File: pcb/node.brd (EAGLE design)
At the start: 50 x 68.5 mm, 14 parts, among them J1 RJ11, J2 RJ11

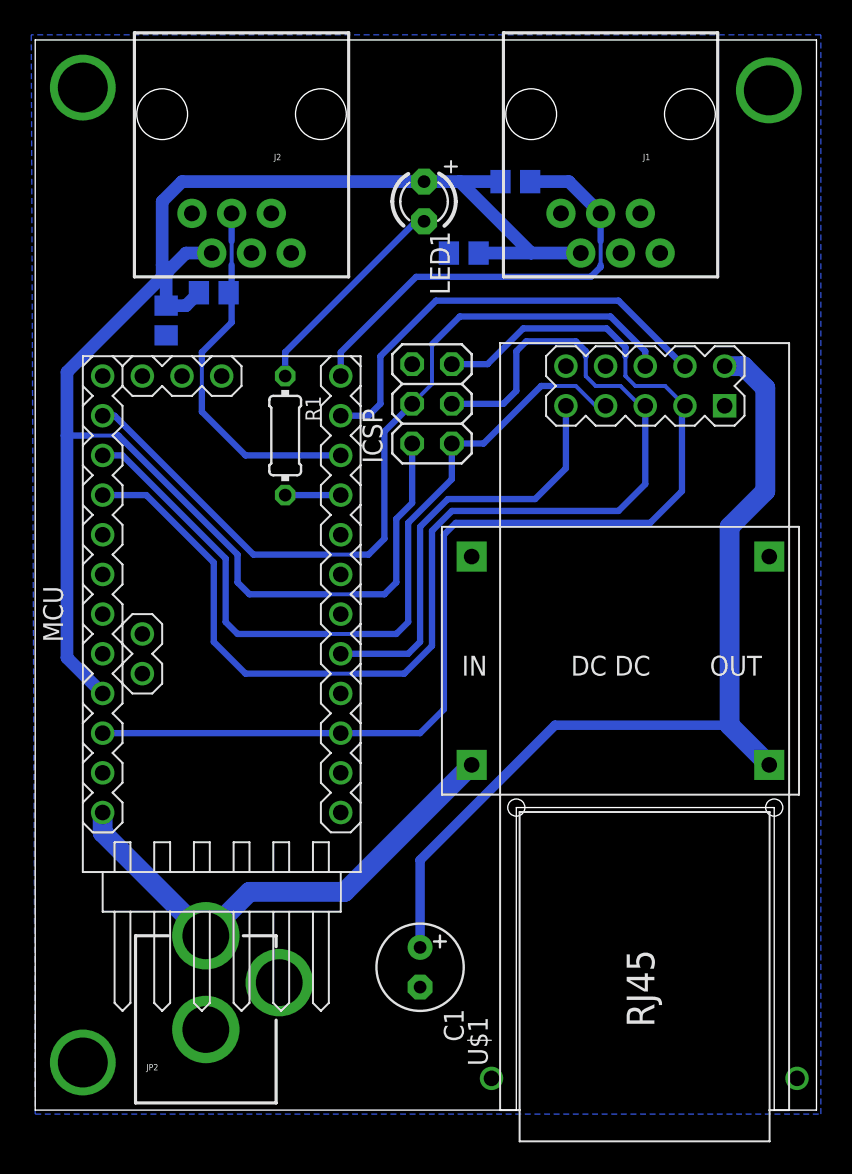
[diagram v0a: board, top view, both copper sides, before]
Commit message: New two layer board version (dirtypcbs.com).
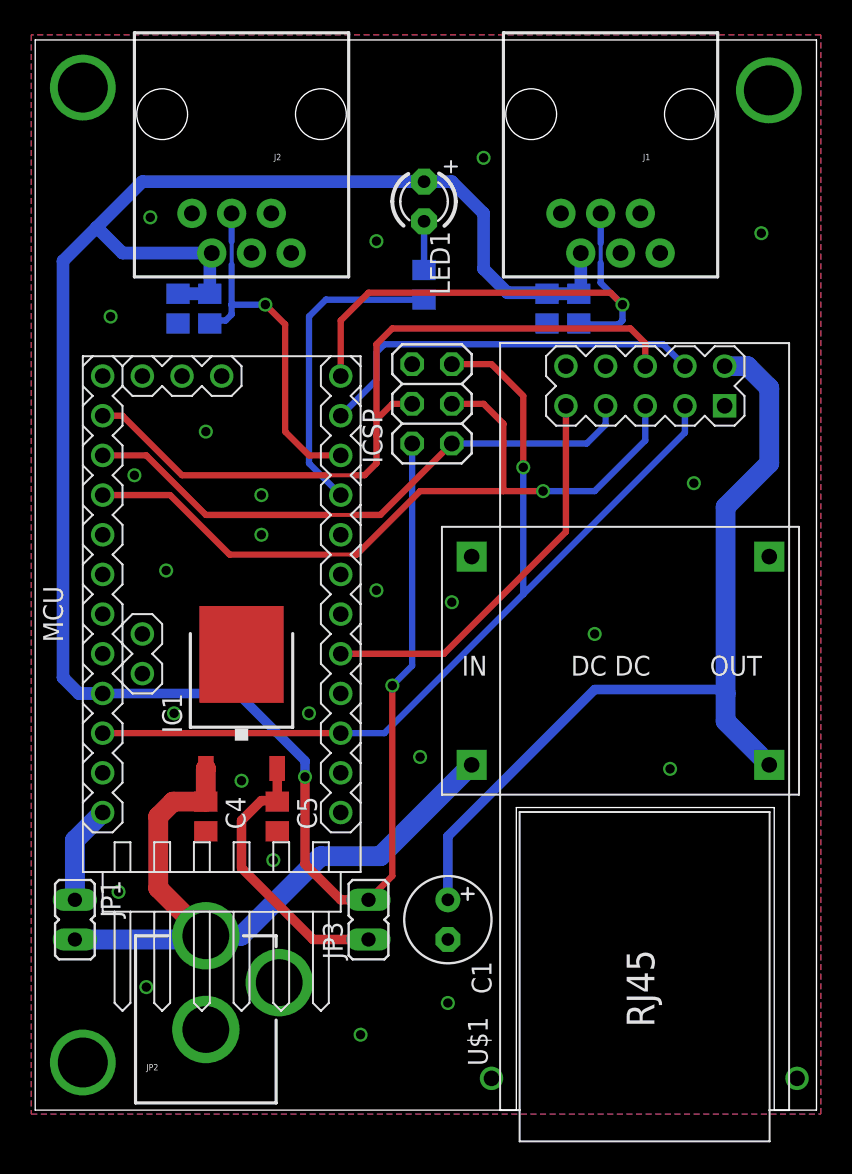
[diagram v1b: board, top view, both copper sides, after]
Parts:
- added C4: 300nF, rcl:C0805
- added C5: 100nF, rcl:C0805
- added IC1: 7805DT, linear:TO252
- added JP1, JP3: (no value), jumper:JP1
- R1: device rcl:0204/7 -> rcl:R0805
- moved R1 13.1 mm to (24.9, 52.8), flipped to the bottom
- moved R2 9.09 mm to (34.8, 51.3), turned to 90 degrees
- moved C3 6.41 mm to (32.8, 51.3), turned to 270 degrees
- moved C1 3.53 mm to (26.4, 12.2)
- moved C2 1.08 mm to (9.14, 51.3)
- moved R3 1.05 mm to (11.2, 51.3), turned to 90 degrees
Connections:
- new net N$2: JP1.1, MCU.J6.1
- new net N$3: C5.1, IC1.2, JP3.1
- net +5V: now also JP3.2
- net GND: now also C4.2, C5.2, IC1.3
- net VIN: now also C4.1, IC1.1, JP1.2; no longer MCU.J6.1
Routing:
- net +5V: track 115.3 -> 141.9 mm, vias 0 -> 2
- net SCK: track 75.0 -> 49.7 mm, vias 0 -> 1
- net N$3: track 0.00 -> 18.0 mm
- net LED_SINK: track 3.56 -> 20.1 mm
- net MISO: track 51.5 -> 37.4 mm
- net VIN: track 32.2 -> 44.5 mm
- net N$1: track 13.9 -> 3.11 mm
- net RESET: track 74.6 -> 65.1 mm, vias 0 -> 1
- net N$2: track 0.00 -> 6.32 mm
- net DHT0_SIG: track 29.2 -> 33.0 mm, vias 0 -> 1
- net ENC28J60_CS: track 28.6 -> 25.5 mm
- net MOSI: track 52.1 -> 49.2 mm
- net +3V3: track 58.3 -> 55.7 mm
- net ENC28J60_DATA_INT: track 27.6 -> 25.7 mm
- net DHT1_SIG: track 23.9 -> 23.1 mm, vias 0 -> 1
- added copper zone on layer 1, net GND
